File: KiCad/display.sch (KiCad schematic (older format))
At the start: 72 parts, among them IC11 SN74LV1T125DCKR, IC6 PCA9517ADP, J1 685119136923, J2 2129320-3, T1 BSS138APW

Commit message: Change HDMI connector on schematic
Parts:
- removed J1: 685119136923, jetson-nano-baseboard-footprints:WE_685119136923, symbol jetson-nano-baseboard:WE_685119136923
- added C81, C82: C_4u7_0402, jetson-nano-baseboard-footprints:0402-cap, symbol jetson-nano-baseboard:C_4u7_0402
- added D16: 1N4148WS, jetson-nano-baseboard-footprints:SOD-323, symbol jetson-nano-baseboard:diode
- added J1: 46756-1001, antmicro-footprints:HDMI_Micro-D_Molex_46765-1x01, symbol antmicroUSBDVIHDMIConnectors:46756-1001
- added R117: R_2k_0402, jetson-nano-baseboard-footprints:0402-res, symbol jetson-nano-baseboard:R_2k_0402
- added R94: R_0R_0402, jetson-nano-baseboard-footprints:0402-res, symbol jetson-nano-baseboard:R_0R_0402
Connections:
- wire segments 268 -> 294
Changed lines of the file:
@@
-$EndComp
-$Comp
-L jetson-nano-baseboard:WE_685119136923 J1
-U 1 1 5E7104B3
-P 14150 1775
-F 0 "J1" H 14152 1943 60  0000 L BNN
-F 1 "685119136923" H 14147 1828 60  0000 L BNN
-F 2 "jetson-nano-baseboard-footprints:WE_685119136923" H 14150 1775 60  0001 C CNN
-F 3 "" H 14150 1775 60  0001 C CNN
-F 4 "Wurth Elektronik" V 2050 1382 60  0001 C CNN "Manufacturer"
-F 5 "685119136923" H -14448 -16328 50  0001 C CNN "MPN"
-	1    14150 1775
-	1    0    0    -1
 $EndComp
 $Comp
@@
 	-1   0    0    1
 $EndComp
+$Comp
+L antmicroUSBDVIHDMIConnectors:46756-1001 J1
+U 1 1 616F319B
+P 14350 2825
+F 0 "J1" H 14780 2962 50  0000 L CNN
+F 1 "46756-1001" H 14780 2871 50  0000 L CNN
+F 2 "antmicro-footprints:HDMI_Micro-D_Molex_46765-1x01" H 14350 2825 50  0001 C CNN
+F 3 "https://www.molex.com/webdocs/datasheets/pdf/en-us/0467651001_IO_CONNECTORS.pdf" H 14350 2825 50  0001 C CNN
+F 4 "467651001" H 14780 2780 50  0000 L CNN "MPN"
+F 5 "Molex" H 14780 2689 50  0000 L CNN "Manufacturer"
+	1    14350 2825
+	1    0    0    -1
+$EndComp
+Text Label 10925 -775 0    60   ~ 0
+TMDS_HPD_IN
+Text Label 10925 -2375 0    60   ~ 0
+TMDS_D2_C_N
+Text Label 10925 -2175 0    60   ~ 0
+TMDS_D1_C_P
+Text Label 10925 -1875 0    60   ~ 0
+TMDS_D0_C_P
+Text Label 10925 -1775 0    60   ~ 0
+TMDS_D0_C_N
+Text Label 10925 -1475 0    60   ~ 0
+TMDS_CLK_C_N
+Text Label 10925 -1575 0    60   ~ 0
+TMDS_CLK_C_P
+Text Label 10925 -2075 0    60   ~ 0
+TMDS_D1_C_N
+Text Label 10925 -1075 0    60   ~ 0
+TMDS_SDA_5V0
+Text Label 10925 -1175 0    60   ~ 0
+TMDS_SCL_5V0
+Text GLabel 11650 -675 0    50   Input ~ 0
+HDMI_SHIELD
+$Comp
+L jetson-nano-baseboard:GND #GND_0152
+U 1 1 618469BA
+P 12025 -200
+F 0 "#GND_0152" H 12025 -200 20  0001 C CNN
+F 1 "GND" H 12027 -347 30  0000 C CNN
+F 2 "" H 12025 -200 70  0001 C CNN
+F 3 "" H 12025 -200 70  0001 C CNN
+	1    12025 -200
+	1    0    0    -1
+$EndComp
+$Comp
+L jetson-nano-baseboard:GND #GND_0153
+U 1 1 618469C0
+P 11725 -200
+F 0 "#GND_0153" H 11725 -200 20  0001 C CNN
+F 1 "GND" H 11727 -347 30  0000 C CNN
+F 2 "" H 11725 -200 70  0001 C CNN
+F 3 "" H 11725 -200 70  0001 C CNN
+	1    11725 -200
+	1    0    0    -1
+$EndComp
+$Comp
+L jetson-nano-baseboard:diode D16
+U 1 1 618469C8
+P 10025 -875
+F 0 "D16" V 9850 -1075 60  0000 L BNN
+F 1 "1N4148WS" V 9950 -1075 60  0000 L BNN
+F 2 "jetson-nano-baseboard-footprints:SOD-323" H 10225 -1075 60  0001 C CNN
+F 3 "" H 10225 -1075 60  0001 C CNN
+F 4 "1N4148WS" H -15673 -20778 50  0001 C CNN "MPN"
+F 5 "ON Semiconductor" H -15673 -20778 50  0001 C CNN "Manufacturer"
+	1    10025 -875
+	0    1    1    0
+$EndComp
+Text Label 10925 -2475 0    60   ~ 0
+TMDS_D2_C_P
+Text GLabel 9725 -875 0    50   Input ~ 0
+HDMI_PWR
+Wire Wire Line
+	12650 -675 11650 -675
+Wire Wire Line
+	12725 -775 10925 -775
+Wire Wire Line
+	9725 -875 9925 -875
+Text Label 12025 -1275 0    60   ~ 0
+TMDS_CEC_IN
+Wire Wire Line
+	12725 -1075 10925 -1075
+Wire Wire Line
+	12725 -1175 10925 -1175
+Wire Wire Line
+	12725 -1275 12025 -1275
+Wire Wire Line
+	11725 -1375 12725 -1375
+Wire Wire Line
+	12725 -2475 10925 -2475
+Wire Wire Line
+	10925 -2375 12725 -2375
+Wire Wire Line
+	10925 -2175 12725 -2175
+Wire Wire Line
+	12725 -2075 10925 -2075
+Wire Wire Line
+	12725 -1875 10925 -1875
+Wire Wire Line
+	12725 -1775 10925 -1775
+Wire Wire Line
+	12725 -1475 10925 -1475
+Wire Wire Line
+	12725 -1575 10925 -1575
+Wire Wire Line
+	10625 -675 10625 -875
+Wire Wire Line
+	10125 -875 10300 -875
+Connection ~ 10625 -875
+Wire Wire Line
+	10625 -875 12725 -875
+Wire Wire Line
+	10300 -675 10300 -875
+Connection ~ 10300 -875
+Wire Wire Line
+	10300 -875 10625 -875
+Wire Wire Line
+	12025 -1275 12025 -550
+Wire Wire Line
+	12025 -250 12025 -200
+Wire Wire Line
+	11725 -200 11725 -250
+Wire Wire Line
+	11725 -1375 11725 -550
+$Comp
+L jetson-nano-baseboard:R_0R_0402 R94
+U 1 1 61846A03
+P 11725 -400
+F 0 "R94" V 11800 -625 60  0000 L CNN
+F 1 "R_0R_0402" H 11725 -550 60  0001 C CNN
+F 2 "jetson-nano-baseboard-footprints:0402-res" H 11925 -200 60  0001 L CNN
+F 3 "" H 11725 -400 50  0001 C CNN
+F 4 "PANASONIC" H 11925 0   60  0001 L CNN "Manufacturer"
+F 5 "ERJ2GE0R00X" H 11925 -100 60  0001 L CNN "MPN"
+F 6 "0R" V 11700 -550 50  0000 L CNN "Val"
+F 7 "DNP" V 11625 -600 50  0000 L CNN "DNP"
+	1    11725 -400
+	0    -1   -1   0
+$EndComp
+$Comp
+L jetson-nano-baseboard:R_2k_0402 R117
+U 1 1 61846A0D
+P 12025 -400
+F 0 "R117" V 11934 -330 60  0000 L CNN
+F 1 "R_2k_0402" H 12025 -550 60  0001 C CNN
+F 2 "jetson-nano-baseboard-footprints:0402-res" H 12225 -200 60  0001 L CNN
+F 3 "" H 12025 -400 50  0001 C CNN
+F 4 "VISHAY" H 12225 0   60  0001 L CNN "Manufacturer"
+F 5 "CRCW04022K00FKED" H 12225 -100 60  0001 L CNN "MPN"
+F 6 "2k" V 12032 -330 50  0000 L CNN "Val"
+F 7 "DNP" V 12123 -330 50  0000 L CNN "DNP"
+	1    12025 -400
+	0    1    1    0
+$EndComp
+$Comp
+L jetson-nano-baseboard:C_4u7_0402 C82
+U 1 1 618469F9
+P 10625 -525
+F 0 "C82" H 10425 -600 60  0000 L CNN
+F 1 "C_4u7_0402" H 10625 -675 60  0001 C CNN
+F 2 "jetson-nano-baseboard-footprints:0402-cap" H 10825 -325 60  0001 L CNN
+F 3 "" H 10625 -525 50  0001 C CNN
+F 4 "MURATA" H 10825 -125 60  0001 L CNN "Manufacturer"
+F 5 "GRM155R61A475MEAAD" H 10825 -225 60  0001 L CNN "MPN"
+F 6 "4u7" H 10400 -475 50  0000 L CNN "Val"
+	1    10625 -525
+	-1   0    0    1
+$EndComp
+Wire Wire Line
+	10300 -275 10300 -375
+Wire Wire Line
+	10625 -375 10625 -275
+$Comp
+L jetson-nano-baseboard:C_4u7_0402 C81
+U 1 1 618469E3
+P 10300 -525
+F 0 "C81" H 10100 -600 60  0000 L CNN
+F 1 "C_4u7_0402" H 10300 -675 60  0001 C CNN
+F 2 "jetson-nano-baseboard-footprints:0402-cap" H 10500 -325 60  0001 L CNN
+F 3 "" H 10300 -525 50  0001 C CNN
+F 4 "MURATA" H 10500 -125 60  0001 L CNN "Manufacturer"
+F 5 "GRM155R61A475MEAAD" H 10500 -225 60  0001 L CNN "MPN"
+F 6 "4u7" H 10075 -475 50  0000 L CNN "Val"
+	1    10300 -525
+	-1   0    0    1
+$EndComp
+$Comp
+L jetson-nano-baseboard:GND #GND_0154
+U 1 1 618469B4
+P 10625 -275
+F 0 "#GND_0154" H 10625 -275 20  0001 C CNN
+F 1 "GND" H 10627 -422 30  0000 C CNN
+F 2 "" H 10625 -275 70  0001 C CNN
+F 3 "" H 10625 -275 70  0001 C CNN
+	1    10625 -275
+	1    0    0    -1
+$EndComp
+$Comp
+L jetson-nano-baseboard:GND #GND_0155
+U 1 1 618469AE
+P 10300 -275
+F 0 "#GND_0155" H 10300 -275 20  0001 C CNN
+F 1 "GND" H 10302 -422 30  0000 C CNN
+F 2 "" H 10300 -275 70  0001 C CNN
+F 3 "" H 10300 -275 70  0001 C CNN
+	1    10300 -275
+	1    0    0    -1
+$EndComp
 $EndSCHEMATC

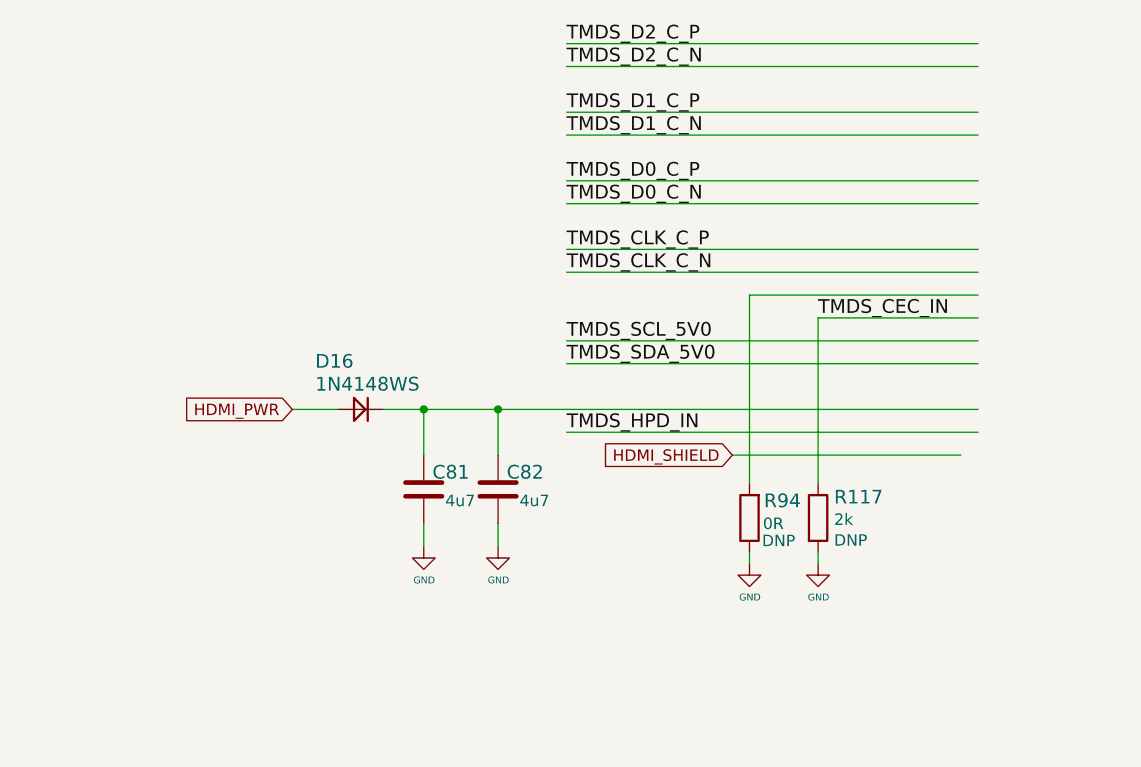
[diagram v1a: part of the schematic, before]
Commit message: Clean copied parts
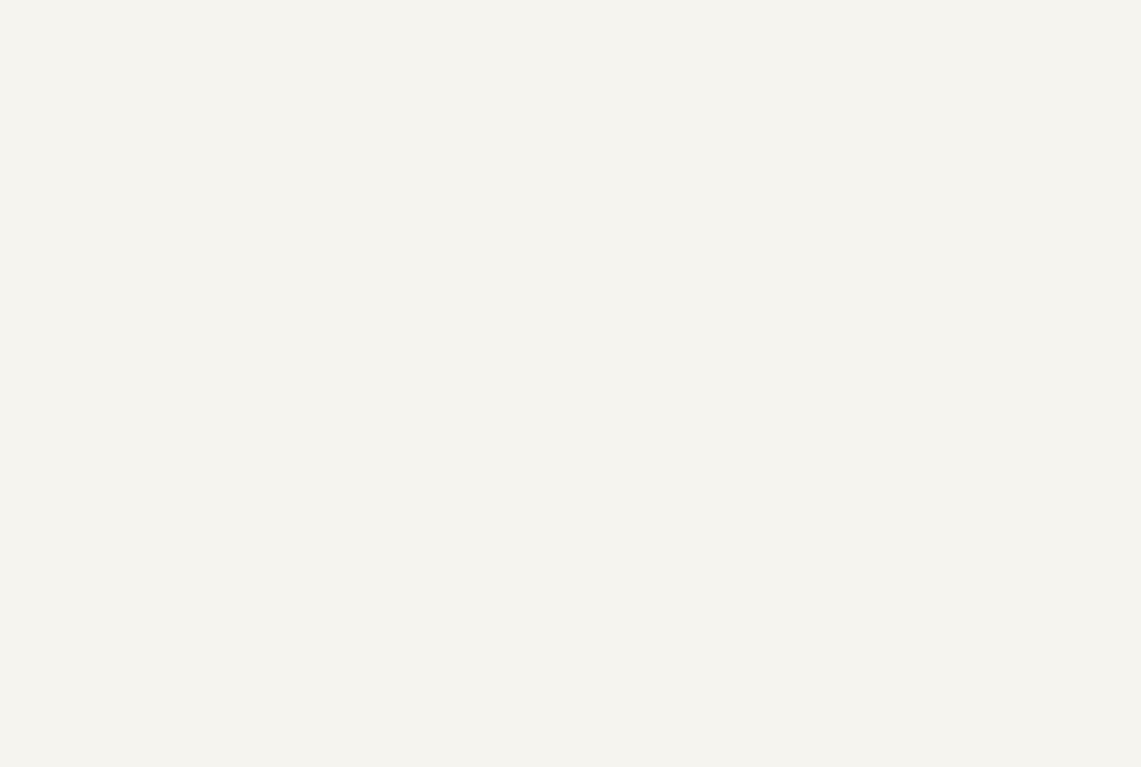
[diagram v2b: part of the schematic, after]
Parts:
- removed C81, C82: C_4u7_0402, jetson-nano-baseboard-footprints:0402-cap, symbol jetson-nano-baseboard:C_4u7_0402
- removed D16: 1N4148WS, jetson-nano-baseboard-footprints:SOD-323, symbol jetson-nano-baseboard:diode
- removed R117: R_2k_0402, jetson-nano-baseboard-footprints:0402-res, symbol jetson-nano-baseboard:R_2k_0402
- removed R94: R_0R_0402, jetson-nano-baseboard-footprints:0402-res, symbol jetson-nano-baseboard:R_0R_0402
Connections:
- wire segments 294 -> 268
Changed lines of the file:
@@
-	1    0    0    -1
-$EndComp
-Text Label 10925 -775 0    60   ~ 0
-TMDS_HPD_IN
-Text Label 10925 -2375 0    60   ~ 0
-TMDS_D2_C_N
-Text Label 10925 -2175 0    60   ~ 0
-TMDS_D1_C_P
-Text Label 10925 -1875 0    60   ~ 0
-TMDS_D0_C_P
-Text Label 10925 -1775 0    60   ~ 0
-TMDS_D0_C_N
-Text Label 10925 -1475 0    60   ~ 0
-TMDS_CLK_C_N
-Text Label 10925 -1575 0    60   ~ 0
-TMDS_CLK_C_P
-Text Label 10925 -2075 0    60   ~ 0
-TMDS_D1_C_N
-Text Label 10925 -1075 0    60   ~ 0
-TMDS_SDA_5V0
-Text Label 10925 -1175 0    60   ~ 0
-TMDS_SCL_5V0
-Text GLabel 11650 -675 0    50   Input ~ 0
-HDMI_SHIELD
-$Comp
-L jetson-nano-baseboard:GND #GND_0152
-U 1 1 618469BA
-P 12025 -200
-F 0 "#GND_0152" H 12025 -200 20  0001 C CNN
-F 1 "GND" H 12027 -347 30  0000 C CNN
-F 2 "" H 12025 -200 70  0001 C CNN
-F 3 "" H 12025 -200 70  0001 C CNN
-	1    12025 -200
-	1    0    0    -1
-$EndComp
-$Comp
-L jetson-nano-baseboard:GND #GND_0153
-U 1 1 618469C0
-P 11725 -200
-F 0 "#GND_0153" H 11725 -200 20  0001 C CNN
-F 1 "GND" H 11727 -347 30  0000 C CNN
-F 2 "" H 11725 -200 70  0001 C CNN
-F 3 "" H 11725 -200 70  0001 C CNN
-	1    11725 -200
-	1    0    0    -1
-$EndComp
-$Comp
-L jetson-nano-baseboard:diode D16
-U 1 1 618469C8
-P 10025 -875
-F 0 "D16" V 9850 -1075 60  0000 L BNN
-F 1 "1N4148WS" V 9950 -1075 60  0000 L BNN
-F 2 "jetson-nano-baseboard-footprints:SOD-323" H 10225 -1075 60  0001 C CNN
-F 3 "" H 10225 -1075 60  0001 C CNN
-F 4 "1N4148WS" H -15673 -20778 50  0001 C CNN "MPN"
-F 5 "ON Semiconductor" H -15673 -20778 50  0001 C CNN "Manufacturer"
-	1    10025 -875
-	0    1    1    0
-$EndComp
-Text Label 10925 -2475 0    60   ~ 0
-TMDS_D2_C_P
-Text GLabel 9725 -875 0    50   Input ~ 0
-HDMI_PWR
-Wire Wire Line
-	12650 -675 11650 -675
-Wire Wire Line
-	12725 -775 10925 -775
-Wire Wire Line
-	9725 -875 9925 -875
-Text Label 12025 -1275 0    60   ~ 0
-TMDS_CEC_IN
-Wire Wire Line
-	12725 -1075 10925 -1075
-Wire Wire Line
-	12725 -1175 10925 -1175
-Wire Wire Line
-	12725 -1275 12025 -1275
-Wire Wire Line
-	11725 -1375 12725 -1375
-Wire Wire Line
-	12725 -2475 10925 -2475
-Wire Wire Line
-	10925 -2375 12725 -2375
-Wire Wire Line
-	10925 -2175 12725 -2175
-Wire Wire Line
-	12725 -2075 10925 -2075
-Wire Wire Line
-	12725 -1875 10925 -1875
-Wire Wire Line
-	12725 -1775 10925 -1775
-Wire Wire Line
-	12725 -1475 10925 -1475
-Wire Wire Line
-	12725 -1575 10925 -1575
-Wire Wire Line
-	10625 -675 10625 -875
-Wire Wire Line
-	10125 -875 10300 -875
-Connection ~ 10625 -875
-Wire Wire Line
-	10625 -875 12725 -875
-Wire Wire Line
-	10300 -675 10300 -875
-Connection ~ 10300 -875
-Wire Wire Line
-	10300 -875 10625 -875
-Wire Wire Line
-	12025 -1275 12025 -550
-Wire Wire Line
-	12025 -250 12025 -200
-Wire Wire Line
-	11725 -200 11725 -250
-Wire Wire Line
-	11725 -1375 11725 -550
-$Comp
-L jetson-nano-baseboard:R_0R_0402 R94
-U 1 1 61846A03
-P 11725 -400
-F 0 "R94" V 11800 -625 60  0000 L CNN
-F 1 "R_0R_0402" H 11725 -550 60  0001 C CNN
-F 2 "jetson-nano-baseboard-footprints:0402-res" H 11925 -200 60  0001 L CNN
-F 3 "" H 11725 -400 50  0001 C CNN
-F 4 "PANASONIC" H 11925 0   60  0001 L CNN "Manufacturer"
-F 5 "ERJ2GE0R00X" H 11925 -100 60  0001 L CNN "MPN"
-F 6 "0R" V 11700 -550 50  0000 L CNN "Val"
-F 7 "DNP" V 11625 -600 50  0000 L CNN "DNP"
-	1    11725 -400
-	0    -1   -1   0
-$EndComp
-$Comp
-L jetson-nano-baseboard:R_2k_0402 R117
-U 1 1 61846A0D
-P 12025 -400
-F 0 "R117" V 11934 -330 60  0000 L CNN
-F 1 "R_2k_0402" H 12025 -550 60  0001 C CNN
-F 2 "jetson-nano-baseboard-footprints:0402-res" H 12225 -200 60  0001 L CNN
-F 3 "" H 12025 -400 50  0001 C CNN
-F 4 "VISHAY" H 12225 0   60  0001 L CNN "Manufacturer"
-F 5 "CRCW04022K00FKED" H 12225 -100 60  0001 L CNN "MPN"
-F 6 "2k" V 12032 -330 50  0000 L CNN "Val"
-F 7 "DNP" V 12123 -330 50  0000 L CNN "DNP"
-	1    12025 -400
-	0    1    1    0
-$EndComp
-$Comp
-L jetson-nano-baseboard:C_4u7_0402 C82
-U 1 1 618469F9
-P 10625 -525
-F 0 "C82" H 10425 -600 60  0000 L CNN
-F 1 "C_4u7_0402" H 10625 -675 60  0001 C CNN
-F 2 "jetson-nano-baseboard-footprints:0402-cap" H 10825 -325 60  0001 L CNN
-F 3 "" H 10625 -525 50  0001 C CNN
-F 4 "MURATA" H 10825 -125 60  0001 L CNN "Manufacturer"
-F 5 "GRM155R61A475MEAAD" H 10825 -225 60  0001 L CNN "MPN"
-F 6 "4u7" H 10400 -475 50  0000 L CNN "Val"
-	1    10625 -525
-	-1   0    0    1
-$EndComp
-Wire Wire Line
-	10300 -275 10300 -375
-Wire Wire Line
-	10625 -375 10625 -275
-$Comp
-L jetson-nano-baseboard:C_4u7_0402 C81
-U 1 1 618469E3
-P 10300 -525
-F 0 "C81" H 10100 -600 60  0000 L CNN
-F 1 "C_4u7_0402" H 10300 -675 60  0001 C CNN
-F 2 "jetson-nano-baseboard-footprints:0402-cap" H 10500 -325 60  0001 L CNN
-F 3 "" H 10300 -525 50  0001 C CNN
-F 4 "MURATA" H 10500 -125 60  0001 L CNN "Manufacturer"
-F 5 "GRM155R61A475MEAAD" H 10500 -225 60  0001 L CNN "MPN"
-F 6 "4u7" H 10075 -475 50  0000 L CNN "Val"
-	1    10300 -525
-	-1   0    0    1
-$EndComp
-$Comp
-L jetson-nano-baseboard:GND #GND_0154
-U 1 1 618469B4
-P 10625 -275
-F 0 "#GND_0154" H 10625 -275 20  0001 C CNN
-F 1 "GND" H 10627 -422 30  0000 C CNN
-F 2 "" H 10625 -275 70  0001 C CNN
-F 3 "" H 10625 -275 70  0001 C CNN
-	1    10625 -275
-	1    0    0    -1
-$EndComp
-$Comp
-L jetson-nano-baseboard:GND #GND_0155
-U 1 1 618469AE
-P 10300 -275
-F 0 "#GND_0155" H 10300 -275 20  0001 C CNN
-F 1 "GND" H 10302 -422 30  0000 C CNN
-F 2 "" H 10300 -275 70  0001 C CNN
-F 3 "" H 10300 -275 70  0001 C CNN
-	1    10300 -275
 	1    0    0    -1
 $EndComp
